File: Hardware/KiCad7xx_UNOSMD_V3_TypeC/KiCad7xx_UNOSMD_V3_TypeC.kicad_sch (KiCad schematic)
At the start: 77 parts, among them J1 -, J2 PINHD-1X18, J3 USB_C_Receptacle_USB2.0, T1 FDN340P, U1 MC33269ST, U2 LP2985-XXDBVR, U3 ATMEGA16U2, U4 ATMEGAXX8-MUR, U5 LMV358?MM, X1 POWERSUPPLY_DC21MMX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

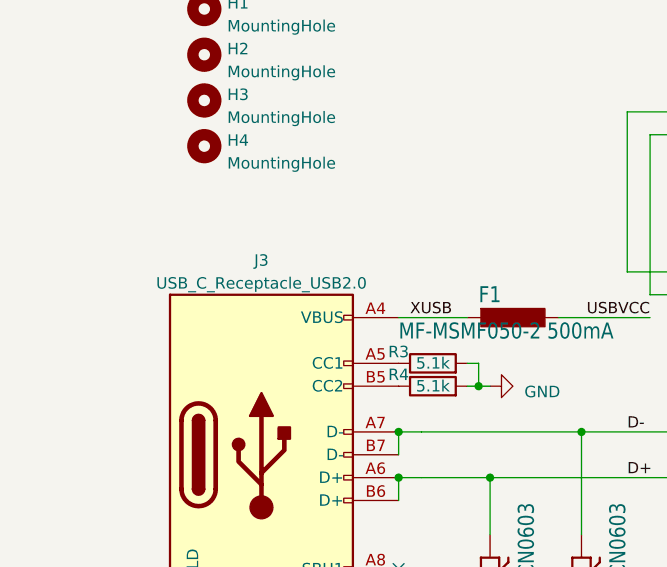
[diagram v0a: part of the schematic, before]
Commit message: Add:TypeC connector was added to the board data.
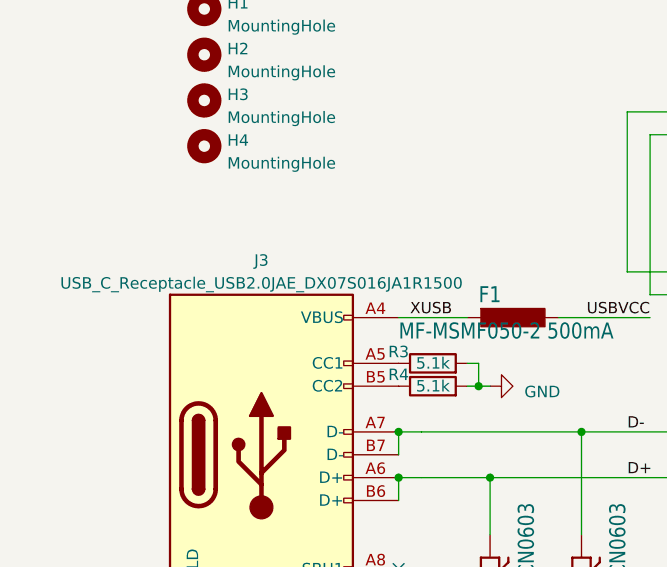
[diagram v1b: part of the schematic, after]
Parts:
- J3: value USB_C_Receptacle_USB2.0 -> USB_C_Receptacle_USB2.0JAE_DX07S016JA1R1500; footprint HRO_TYPE-C-31-M-12:HRO_TYPE-C-31-M-12 -> Connector_USB:USB_C_Receptacle_JAE_DX07S016JA1R1500
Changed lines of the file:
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@@
       (effects (font (size 1.27 1.27)))
     )
-    (property "Value" "USB_C_Receptacle_USB2.0" (at 20.32 135.89 0)
+    (property "Value" "USB_C_Receptacle_USB2.0JAE_DX07S016JA1R1500" (at 20.32 135.89 0)
       (effects (font (size 1.27 1.27)))
     )
-    (property "Footprint" "HRO_TYPE-C-31-M-12:HRO_TYPE-C-31-M-12" (at 24.13 154.94 0)
+    (property "Footprint" "Connector_USB:USB_C_Receptacle_JAE_DX07S016JA1R1500" (at 24.13 154.94 0)
       (effects (font (size 1.27 1.27)) hide)
     )
